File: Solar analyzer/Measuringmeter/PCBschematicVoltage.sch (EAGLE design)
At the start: 8 parts, among them X1 OPAMP

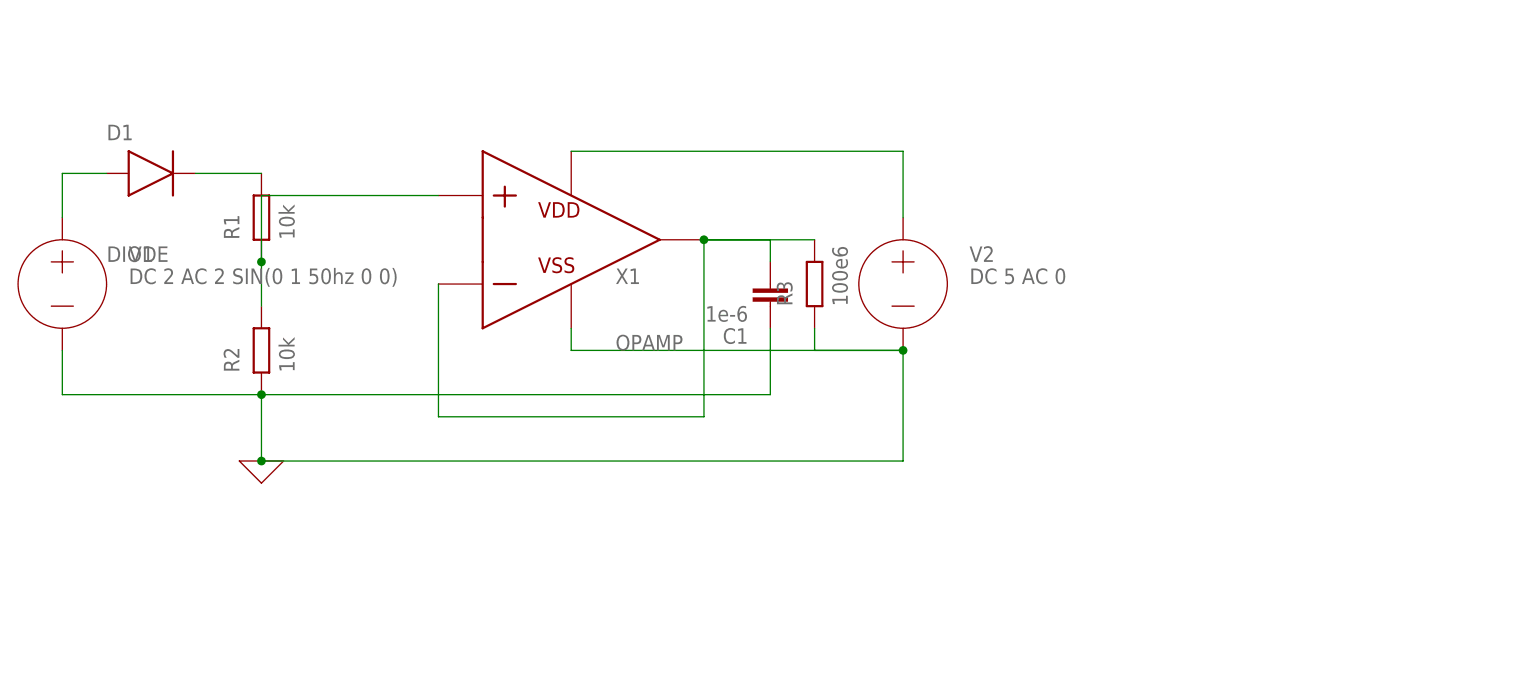
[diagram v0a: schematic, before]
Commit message: Add I2C connection, Opamp for CS
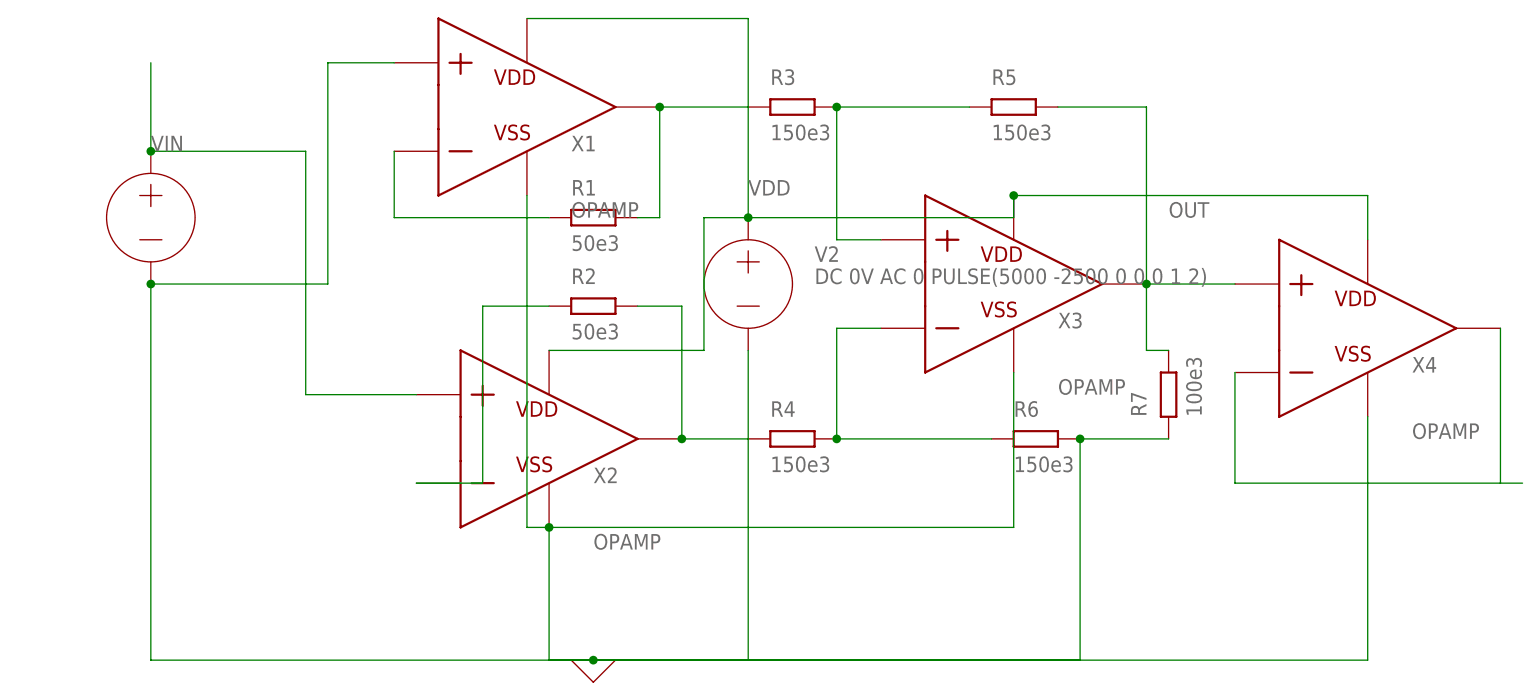
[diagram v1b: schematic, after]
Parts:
- removed C1: 1e-6, ngspice-simulation:C
- removed D1: DIODE, ngspice-simulation:DIODE
- added R4, R5, R6: 150e3, ngspice-simulation:R
- added R7: 100e3, ngspice-simulation:R
- added X2, X3, X4: OPAMP, ngspice-simulation:OPAMP
- R1, R2: value 10k -> 50e3
- R3: value 100e6 -> 150e3
- V1: value DC 2 AC 2 SIN(0 1 50hz 0 0) -> DC 5000 AC 5000 PULSE(5000 0 0 0 0 .5 1)
- V2: value DC 5 AC 0 -> DC 0V AC 0 PULSE(5000 -2500 0 0 0 1 2)
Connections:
- removed net 10K: R1.1, R2.2, X1.P
- removed net N$4: C1.2, R3.2, X1.N, X1.VOUT
- new net N$5: R2.1, X2.N
- new net N$6: R2.2, R4.1, X2.VOUT
- new net N$7: R4.2, R6.1, X3.N
- new net N$8: X4.N, X4.VOUT
- new net OUT: R5.2, R7.2, X3.VOUT, X4.P
- new net VDD: V2.+, X1.VDD, X2.VDD, X3.VDD, X4.VDD
- new net VIN: V1.+, X2.P
- net 0: now also R6.2, R7.1, X1.P, X2.VSS, X3.VSS, X4.VSS; no longer C1.1, R2.1, R3.1
- net N$1: now also R1.1, X1.N; no longer D1.A, V1.+
- net N$2: now also R3.1, X1.VOUT; no longer D1.C
- net N$3: now also R3.2, R5.1, X3.P; no longer V2.+, X1.VDD
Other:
- moved on the sheet: R1, R2, R3, V2, X1
